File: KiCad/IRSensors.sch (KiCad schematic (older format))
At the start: 26 parts, among them U10 GP2Y0E02B, U11 GP2Y0E02B, U12 GP2Y0E02B, U13 GP2Y0E02B, U14 GP2Y0E02B, U15 GP2Y0E02B, U7 TCA9548APWR, U8 GP2Y0E02B, U9 GP2Y0E02B

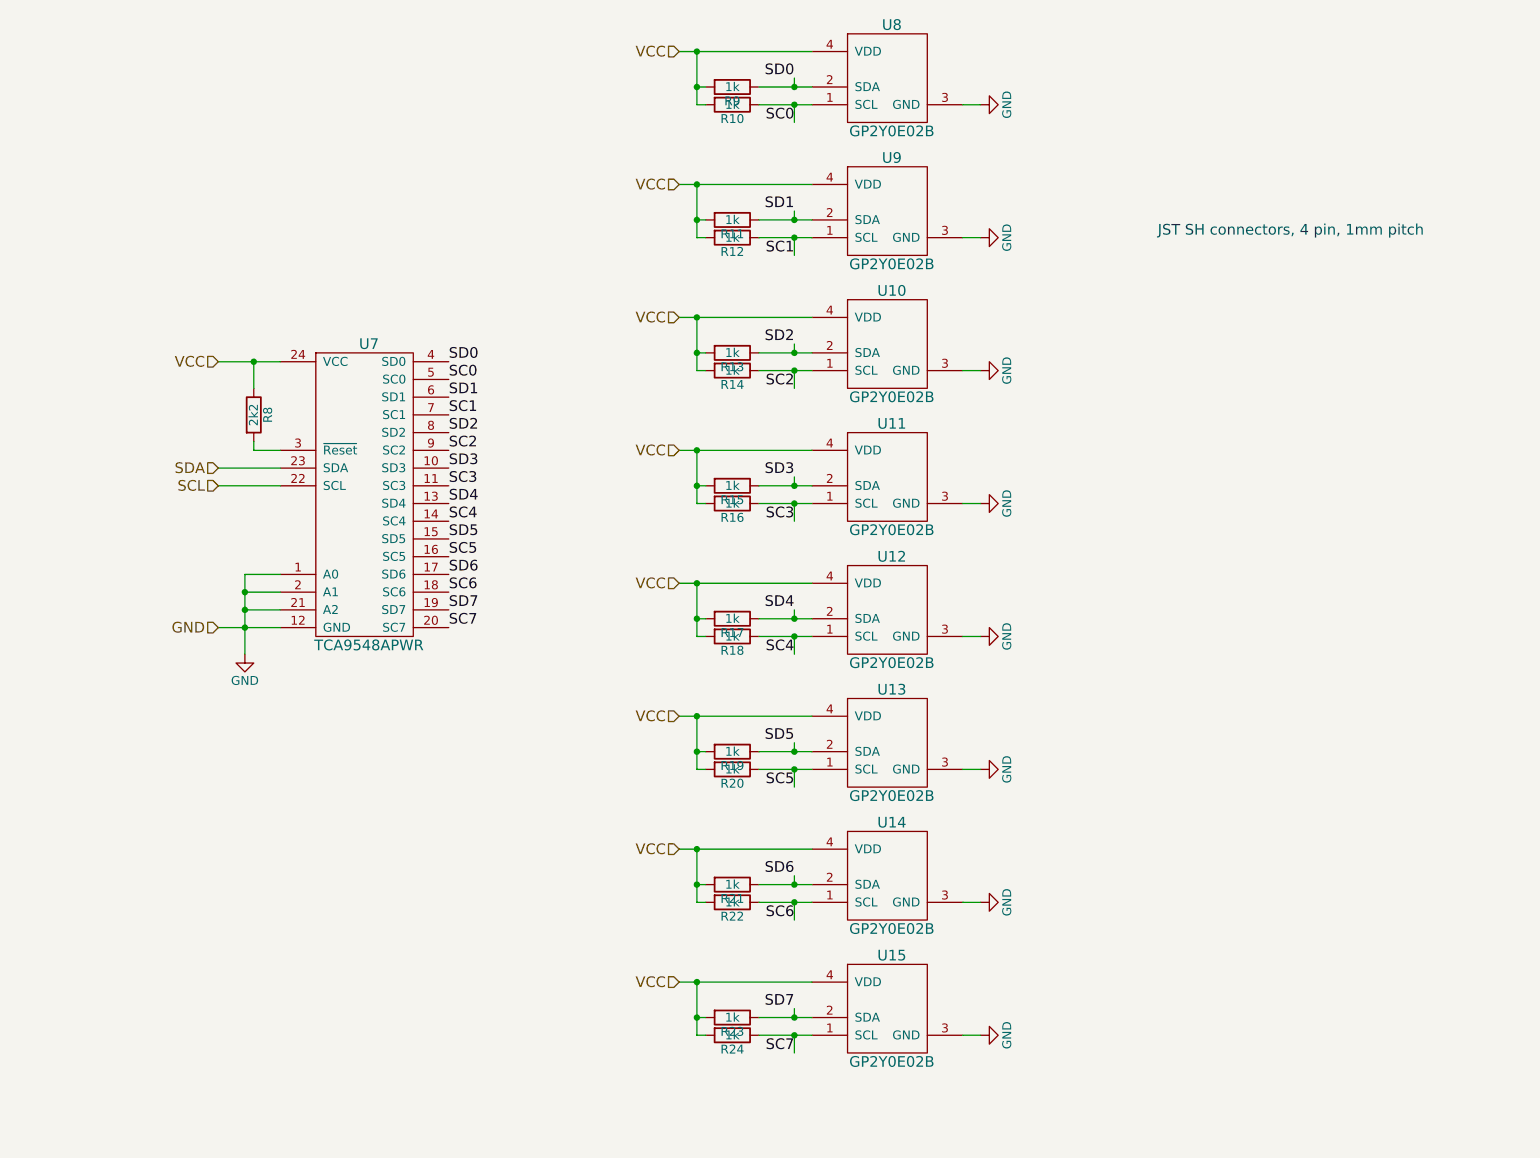
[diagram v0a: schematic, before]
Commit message: Working on PCB layout for Rev 2
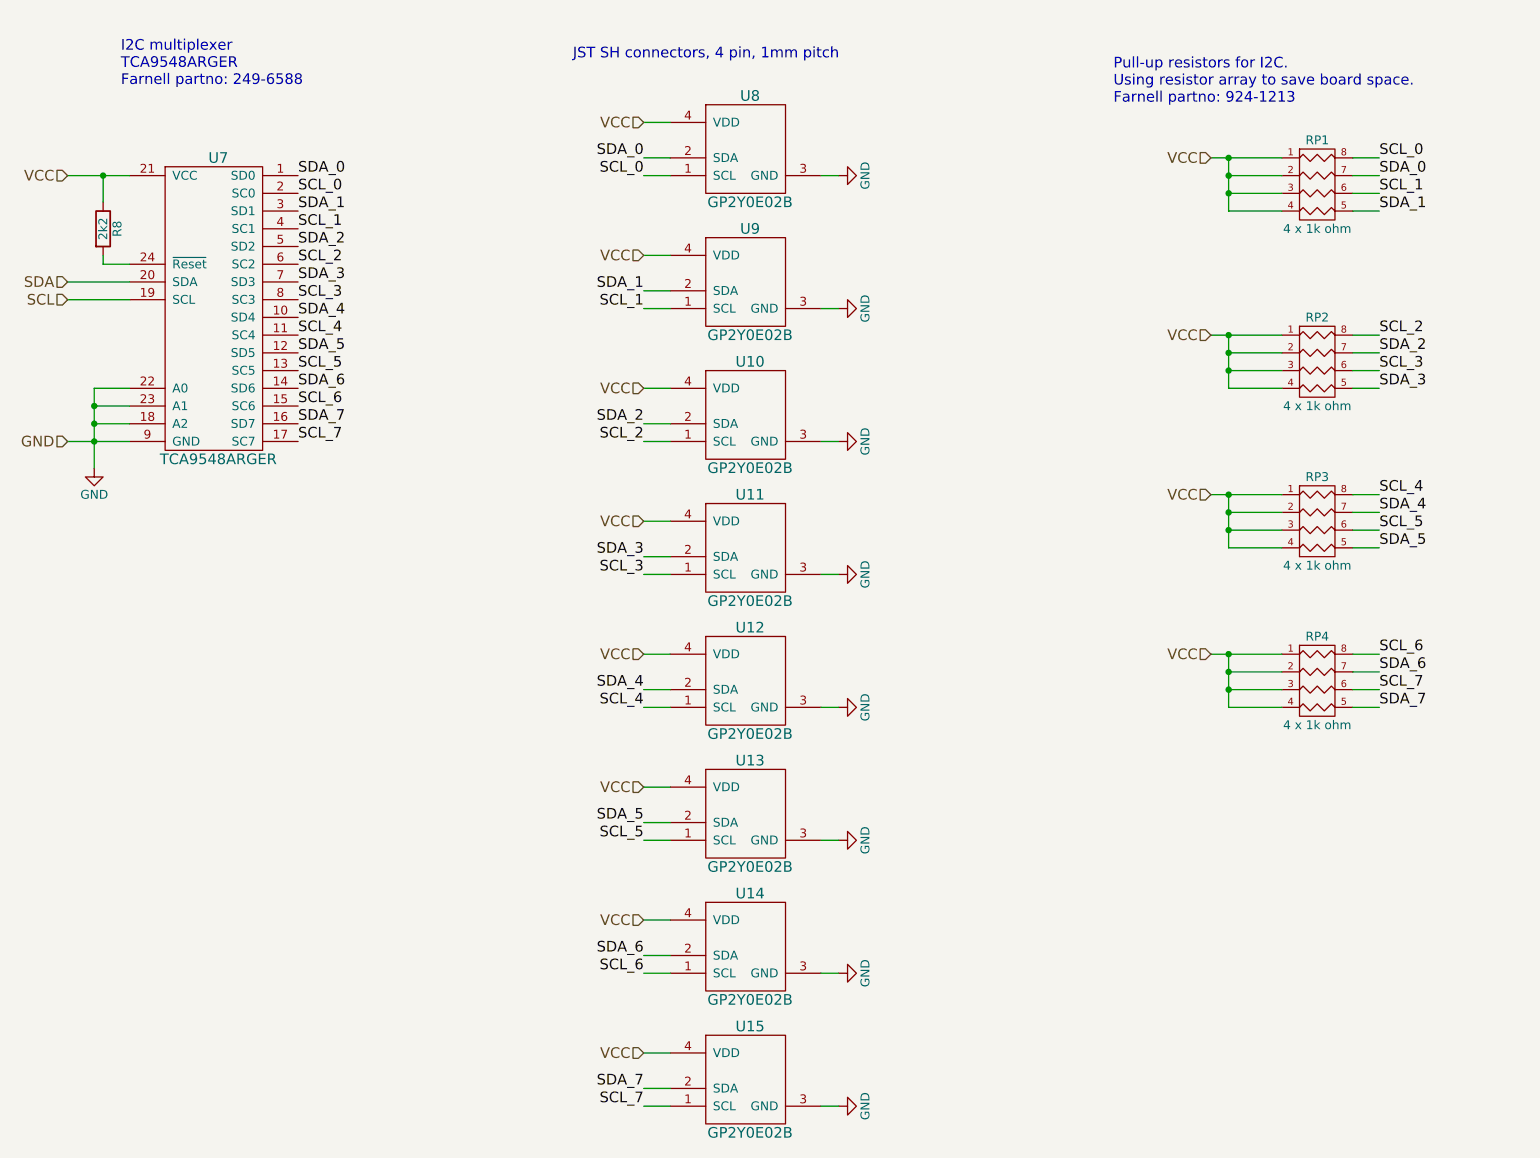
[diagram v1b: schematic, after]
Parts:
- removed R10, R11, R12, R13, R14, R15, R16, R17, R18, R19, R20, R21, R22, R23, R24, R9: 1k, Resistors_SMD:R_0603, symbol R
- removed U7: TCA9548APWR, Housings_SSOP:TSSOP-24_4.4x7.8mm_Pitch0.65mm, symbol TCA9548APWR
- added RP1, RP2, RP3, RP4: 4 x 1k ohm, Resistors_SMD:R_Array_Convex_4x0603, symbol R_PACK4
- added U7: TCA9548ARGER, Housings_DFN_QFN:QFN-24-1EP_4x4mm_Pitch0.5mm, symbol TCA9548ARGER
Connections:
- net GND: now also U7.18 (A2), U7.22 (A0), U7.23 (A1), U7.9 (GND)
- net SCL: now also U7.19 (SCL)
- net SDA: now also U7.20 (SDA)
- net VCC: now also RP1.1 (P1), RP1.2 (P2), RP1.3 (P3), RP1.4 (P4), RP2.1 (P1), RP2.2 (P2), RP2.3 (P3), RP2.4 (P4), RP3.1 (P1), RP3.2 (P2), RP3.3 (P3), RP3.4 (P4), RP4.1 (P1), RP4.2 (P2), RP4.3 (P3), RP4.4 (P4), U7.21 (VCC)
- net at R8.2: now also U7.24 (~Reset)
- net SC0 renamed SCL_0
- net SCL_0: now also RP1.8 (R1), U7.2 (SC0)
- net SC1 renamed SCL_1
- net SCL_1: now also RP1.6 (R3), U7.4 (SC1)
- net SC2 renamed SCL_2
- net SCL_2: now also RP2.8 (R1), U7.6 (SC2)
- net SC3 renamed SCL_3
- net SCL_3: now also RP2.6 (R3), U7.8 (SC3)
- net SC4 renamed SCL_4
- net SCL_4: now also RP3.8 (R1), U7.11 (SC4)
- net SC5 renamed SCL_5
- net SCL_5: now also RP3.6 (R3), U7.13 (SC5)
- net SC6 renamed SCL_6
- net SCL_6: now also RP4.8 (R1), U7.15 (SC6)
- net SC7 renamed SCL_7
- net SCL_7: now also RP4.6 (R3), U7.17 (SC7)
- net SD0 renamed SDA_0
- net SDA_0: now also RP1.7 (R2), U7.1 (SD0)
- net SD1 renamed SDA_1
- net SDA_1: now also RP1.5 (R4), U7.3 (SD1)
- net SD2 renamed SDA_2
- net SDA_2: now also RP2.7 (R2), U7.5 (SD2)
- net SD3 renamed SDA_3
- net SDA_3: now also RP2.5 (R4), U7.7 (SD3)
- net SD4 renamed SDA_4
- net SDA_4: now also RP3.7 (R2), U7.10 (SD4)
- net SD5 renamed SDA_5
- net SDA_5: now also RP3.5 (R4), U7.12 (SD5)
- net SD6 renamed SDA_6
- net SDA_6: now also RP4.7 (R2), U7.14 (SD6)
- net SD7 renamed SDA_7
- net SDA_7: now also RP4.5 (R4), U7.16 (SD7)
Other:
- note added: "I2C multiplexer\nTCA9548ARGER\nFarnell partno: 249-6588"
- note added: "Pull-up resistors for I2C. \nUsing resistor array to save board space.\nFarnell partno: 924-1213"
- moved on the sheet: R8, U8

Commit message: More related to USB
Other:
- note added: "1k pull-up resistors for I2C. \nUsing resistor array to save board space.\nFarnell partno: 923-4519"
- note added: "JST SH connectors, 4 pin, 1mm pitch\nFarnell partno: 167-9129 (top entry) or 183-0839 (right angle)"
- note removed: "JST SH connectors, 4 pin, 1mm pitch"
- note removed: "Pull-up resistors for I2C. \nUsing resistor array to save board space.\nFarnell partno: 924-1213"
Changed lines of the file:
@@
 $Descr A4 11693 8268
 encoding utf-8
-Sheet 3 3
+Sheet 3 4
 Title ""
 Date ""
@@
 	1    0    0    -1
 $EndComp
-Text Notes 4300 1000 0    60   ~ 0
-JST SH connectors, 4 pin, 1mm pitch
+Text Notes 3750 1100 0    60   ~ 0
+JST SH connectors, 4 pin, 1mm pitch\nFarnell partno: 167-9129 (top entry) or 183-0839 (right angle)
 $Comp
 L R_PACK4 RP1
@@
 	8850 1850 8700 1850
 Text Notes 7350 1250 0    60   ~ 0
-Pull-up resistors for I2C. \nUsing resistor array to save board space.\nFarnell partno: 924-1213
+1k pull-up resistors for I2C. \nUsing resistor array to save board space.\nFarnell partno: 923-4519
 Text HLabel 7900 1550 0    60   Input ~ 0
 VCC
@@
 	1    0    0    -1
 $EndComp
-Text Notes 1750 1150 0    60   ~ 0
+Text Notes 1750 1350 0    60   ~ 0
 I2C multiplexer\nTCA9548ARGER\nFarnell partno: 249-6588
 $EndSCHEMATC
